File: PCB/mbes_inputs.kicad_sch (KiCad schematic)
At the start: 10 parts

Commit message: PCB-A size reducing
Now PCB-B and PCB-A fits almost perfectly, but not the pin-header connectors. I will use wires instead. But they can be mnounted A on top of B ;-)
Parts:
- Bike_stand1, Decomp_1, LightOnOff_sw1, addLights1, powerOFF1: footprint Connector_Wire:SolderWire-0.5sqmm_1x02_P4.6mm_D0.9mm_OD2.1mm -> Connector_Wire:SolderWire-0.25sqmm_1x02_P4.2mm_D0.65mm_OD1.7mm
- leftCtrls_conn1: footprint Connector_Wire:SolderWire-0.5sqmm_1x06_P4.6mm_D0.9mm_OD2.1mm -> Connector_Wire:SolderWire-0.25sqmm_1x06_P4.5mm_D0.65mm_OD2mm
- rightCtrls_conn1: footprint Connector_Wire:SolderWire-0.5sqmm_1x06_P4.6mm_D0.9mm_OD2.1mm -> Connector_Wire:SolderWire-0.25sqmm_1x06_P4.2mm_D0.65mm_OD1.7mm
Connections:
- net GND: now also powerOFF1.1 (Pin_1)
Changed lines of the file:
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@@
   (junction (at 65.786 67.564) (diameter 0) (color 0 0 0 0)
   )
+  (junction (at 65.7606 148.9456) (diameter 0) (color 0 0 0 0)
+  )
   (junction (at 98.298 135.89) (diameter 0) (color 0 0 0 0)
   )
@@
     (stroke (width 0) (type default))
   )
+  (wire (pts (xy 65.7606 148.9456) (xy 65.786 148.9456))
+    (stroke (width 0) (type default))
+  )
   (wire (pts (xy 93.472 121.793) (xy 95.504 121.793))
     (stroke (width 0) (type default))
@@
     (stroke (width 0) (type default))
   )
-  (wire (pts (xy 65.786 122.428) (xy 65.786 148.9964))
-    (stroke (width 0) (type default))
-  )
-  (wire (pts (xy 61.6712 148.9456) (xy 65.786 148.9456))
+  (wire (pts (xy 65.786 122.428) (xy 65.786 148.9456))
+    (stroke (width 0) (type default))
+  )
+  (wire (pts (xy 61.6712 148.9456) (xy 65.7606 148.9456))
     (stroke (width 0) (type default))
   )
@@
       (effects (font (size 1.27 1.27)) hide)
     )
-    (property "Footprint" "Connector_Wire:SolderWire-0.5sqmm_1x02_P4.6mm_D0.9mm_OD2.1mm" (at 56.642 67.564 0)
+    (property "Footprint" "Connector_Wire:SolderWire-0.25sqmm_1x02_P4.2mm_D0.65mm_OD1.7mm" (at 56.642 67.564 0)
       (effects (font (size 1.27 1.27)) hide)
     )
@@
       (effects (font (size 1.27 1.27)) (justify left) hide)
     )
-    (property "Footprint" "Connector_Wire:SolderWire-0.5sqmm_1x02_P4.6mm_D0.9mm_OD2.1mm" (at 56.896 116.84 0)
+    (property "Footprint" "Connector_Wire:SolderWire-0.25sqmm_1x02_P4.2mm_D0.65mm_OD1.7mm" (at 56.896 116.84 0)
       (effects (font (size 1.27 1.27)) hide)
     )
@@
     )
   )
-  (symbol (lib_id "power:GND") (at 65.786 148.9964 0) (unit 1)
+  (symbol (lib_id "power:GND") (at 65.7606 148.9456 0) (unit 1)
     (in_bom yes) (on_board yes) (dnp no) (fields_autoplaced)
-    (property "Reference" "#PWR0108" (at 65.786 155.3464 0)
-      (effects (font (size 1.27 1.27)) hide)
-    )
-    (property "Value" "GND" (at 65.786 154.0764 0)
-      (effects (font (size 1.27 1.27)))
-    )
-    (property "Footprint" "" (at 65.786 148.9964 0)
-      (effects (font (size 1.27 1.27)) hide)
-    )
-    (property "Datasheet" "" (at 65.786 148.9964 0)
+    (property "Reference" "#PWR0108" (at 65.7606 155.2956 0)
+      (effects (font (size 1.27 1.27)) hide)
+    )
+    (property "Value" "GND" (at 65.7606 154.0256 0)
+      (effects (font (size 1.27 1.27)))
+    )
+    (property "Footprint" "" (at 65.7606 148.9456 0)
+      (effects (font (size 1.27 1.27)) hide)
+    )
+    (property "Datasheet" "" (at 65.7606 148.9456 0)
       (effects (font (size 1.27 1.27)) hide)
     )
@@
       (effects (font (size 1.27 1.27)))
     )
-    (property "Footprint" "Connector_Wire:SolderWire-0.5sqmm_1x06_P4.6mm_D0.9mm_OD2.1mm" (at 56.642 83.312 0)
+    (property "Footprint" "Connector_Wire:SolderWire-0.25sqmm_1x06_P4.5mm_D0.65mm_OD2mm" (at 56.642 83.312 0)
       (effects (font (size 1.27 1.27)) hide)
     )
@@
       (effects (font (size 1.27 1.27)) (justify left) hide)
     )
-    (property "Footprint" "Connector_Wire:SolderWire-0.5sqmm_1x02_P4.6mm_D0.9mm_OD2.1mm" (at 56.642 100.584 0)
+    (property "Footprint" "Connector_Wire:SolderWire-0.25sqmm_1x02_P4.2mm_D0.65mm_OD1.7mm" (at 56.642 100.584 0)
       (effects (font (size 1.27 1.27)) hide)
     )
@@
       (effects (font (size 1.27 1.27)) hide)
     )
-    (property "Footprint" "Connector_Wire:SolderWire-0.5sqmm_1x02_P4.6mm_D0.9mm_OD2.1mm" (at 56.896 122.428 0)
+    (property "Footprint" "Connector_Wire:SolderWire-0.25sqmm_1x02_P4.2mm_D0.65mm_OD1.7mm" (at 56.896 122.428 0)
       (effects (font (size 1.27 1.27)) hide)
     )
@@
       (effects (font (size 1.27 1.27)))
     )
-    (property "Footprint" "Connector_Wire:SolderWire-0.5sqmm_1x06_P4.6mm_D0.9mm_OD2.1mm" (at 56.642 50.292 0)
+    (property "Footprint" "Connector_Wire:SolderWire-0.25sqmm_1x06_P4.2mm_D0.65mm_OD1.7mm" (at 56.642 50.292 0)
       (effects (font (size 1.27 1.27)) hide)
     )
@@
       (effects (font (size 1.27 1.27)) (justify left) hide)
     )
-    (property "Footprint" "Connector_Wire:SolderWire-0.5sqmm_1x02_P4.6mm_D0.9mm_OD2.1mm" (at 56.5912 148.9456 0)
-      (effects (font (size 1.27 1.27)) hide)
-    )
+    (property "Footprint" "Connector_Wire:SolderWire-0.25sqmm_1x02_P4.2mm_D0.65mm_OD1.7mm" (at 56.5912 148.9456 0)
+      (effects (font (size 1.27 1.27)) hide)
+    )

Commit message: Size reducing and component rationalization
- RS232(TTL) lines on PCB-B have been removed (MAX232 is already mounted in PCB-A)
- The two PCB can no more be connected using pin-header connectors. You have to use welded wires, now.
  (this solution is not beautiful as the original, but it is a more flexible one and it also allowd me
  to reduce the PCB size)

The PCBs size is approximately 109.7mm x 43.5mm.
For this dual-face sigle-layer (THT) version this is the minimum size I can achieve.
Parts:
- Bike_stand1, Decomp_1, LightOnOff_sw1, addLights1, powerOFF1: footprint Connector_Wire:SolderWire-0.25sqmm_1x02_P4.2mm_D0.65mm_OD1.7mm -> Connector_Wire:SolderWire-0.15sqmm_1x02_P4mm_D0.5mm_OD1.5mm
- leftCtrls_conn1: footprint Connector_Wire:SolderWire-0.25sqmm_1x06_P4.5mm_D0.65mm_OD2mm -> Connector_Wire:SolderWire-0.25sqmm_1x06_P4.2mm_D0.65mm_OD1.7mm
- rightCtrls_conn1: footprint Connector_Wire:SolderWire-0.25sqmm_1x06_P4.2mm_D0.65mm_OD1.7mm -> Connector_Wire:SolderWire-0.15sqmm_1x06_P4mm_D0.5mm_OD1.5mm

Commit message: Tuning and fixes
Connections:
- net i_Vx1: now also Key-locker-1.3 (Pin_3); no longer Key-locker-1.2 (Pin_2)
- net i_Vx2: now also Key-locker-1.1 (Pin_1); no longer Key-locker-1.4 (Pin_4)
- new net: Key-locker-1.2 (Pin_2), Key-locker-1.4 (Pin_4), R1.2
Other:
- moved on the sheet: Key-locker-1
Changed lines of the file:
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@@
 	(symbol
 		(lib_id "Connector_Generic:Conn_01x04")
-		(at 56.896 133.35 0)
-		(mirror y)
+		(at 56.896 135.89 180)
 		(unit 1)
 		(exclude_from_sim no)
@@
 		(dnp no)
 		(property "Reference" "Key-locker-1"
-			(at 57.3532 128.1176 0)
+			(at 56.642 128.016 0)
 			(effects
 				(font
@@
 		)
 		(property "Value" "Conn_01x04"
-			(at 56.896 142.5956 0)
+			(at 56.896 126.6444 0)
 			(effects
 				(font
@@
 		)
 		(property "Footprint" "Connector_PinHeader_2.54mm:PinHeader_1x04_P2.54mm_Vertical"
-			(at 56.896 133.35 0)
+			(at 56.896 135.89 0)
 			(effects
 				(font
@@
 		)
 		(property "Datasheet" "~"
-			(at 56.896 133.35 0)
+			(at 56.896 135.89 0)
 			(effects
 				(font
@@
 		)
 		(property "Description" ""
-			(at 56.896 133.35 0)
+			(at 56.896 135.89 0)
 			(effects
 				(font

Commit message: Important fixes and adjustments
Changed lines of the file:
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@@
-	)
-	(junction
-		(at 98.298 135.89)
-		(diameter 0)
-		(color 0 0 0 0)
 	)
 	(junction
@@
 	(wire
 		(pts
-			(xy 75.946 135.89) (xy 98.298 135.89)
-		)
-		(stroke
-			(width 0)
-			(type default)
-		)
-	)
-	(wire
-		(pts
 			(xy 91.44 133.35) (xy 91.44 118.491)
 		)
@@
 	(wire
 		(pts
-			(xy 98.298 135.89) (xy 101.727 135.89)
+			(xy 75.946 135.89) (xy 101.727 135.89)
 		)
 		(stroke
@@
 					(unit 1)
 				)
-			)
-		)
-	)
-	(symbol
-		(lib_id "power:PWR_FLAG")
-		(at 98.298 135.89 0)
-		(unit 1)
-		(exclude_from_sim no)
-		(in_bom yes)
-		(on_board yes)
-		(dnp no)
-		(fields_autoplaced yes)
-		(property "Reference" "#FLG0103"
-			(at 98.298 133.985 0)
-			(effects
-				(font
-					(size 1.27 1.27)
-				)
-				(hide yes)
-			)
-		)
-		(property "Value" "PWR_FLAG"
-			(at 98.298 131.318 0)
-			(effects
-				(font
-					(size 1.27 1.27)
-				)
-			)
-		)
-		(property "Footprint" ""
-			(at 98.298 135.89 0)
-			(effects
-				(font
-					(size 1.27 1.27)
-				)
-				(hide yes)
-			)
-		)
-		(property "Datasheet" "~"
-			(at 98.298 135.89 0)
-			(effects
-				(font
-					(size 1.27 1.27)
-				)
-				(hide yes)
-			)
-		)
-		(property "Description" ""
-			(at 98.298 135.89 0)
-			(effects
-				(font
-					(size 1.27 1.27)
-				)
-				(hide yes)
-			)
-		)
-		(pin "1"
-		)
-		(instances
-			(project "pcb-a"
-				(path "/709d0967-afe5-49d3-92a5-d2bb94550bdb/0b22d592-b723-42a2-89dd-bec665c2bd26"
-					(reference "#FLG0103")
-					(unit 1)
-				)

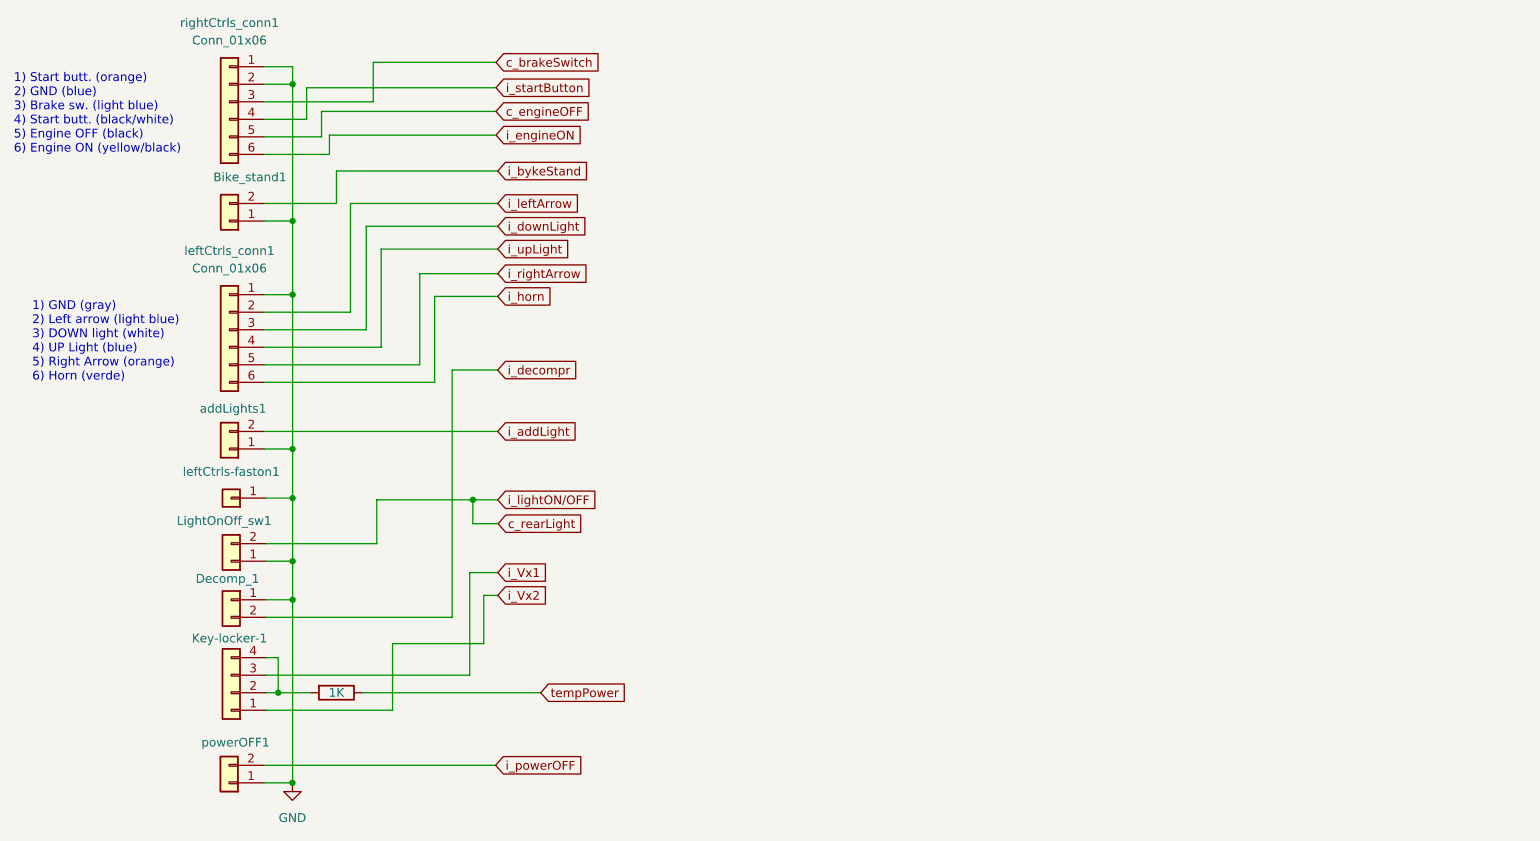
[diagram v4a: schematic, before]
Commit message: Bike-stand switch moved in the rear-connector
All connectors have been placed in one single sheet
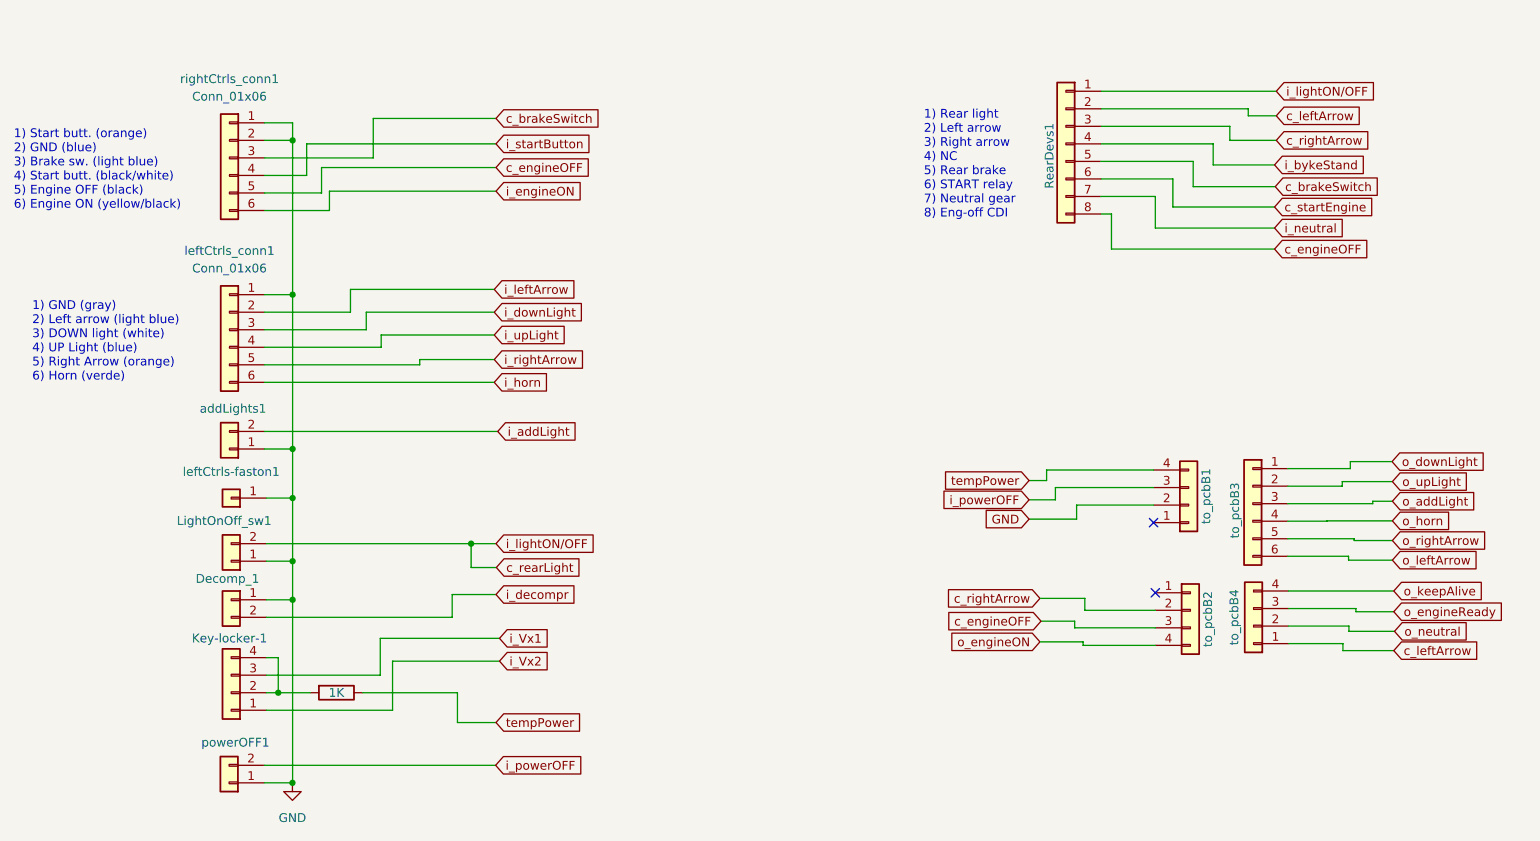
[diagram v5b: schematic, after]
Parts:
- removed Bike_stand1: Conn_01x02, Connector_Wire:SolderWire-0.15sqmm_1x02_P4mm_D0.5mm_OD1.5mm, symbol Connector_Generic:Conn_01x02
- added RearDevs1: Conn_01x08, Connector_PinHeader_2.54mm:PinHeader_1x08_P2.54mm_Vertical, symbol Connector_Generic:Conn_01x08
- added to_pcbB1, to_pcbB2, to_pcbB4: Conn_01x04, Connector_PinHeader_2.54mm:PinHeader_1x04_P2.54mm_Vertical, symbol Connector_Generic:Conn_01x04
- added to_pcbB3: Conn_01x06, Connector_PinHeader_2.54mm:PinHeader_1x06_P2.54mm_Vertical, symbol Connector_Generic:Conn_01x06
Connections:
- net GND: now also to_pcbB1.2 (Pin_2)
- net c_brakeSwitch: now also RearDevs1.5 (Pin_5)
- net c_engineOFF: now also RearDevs1.8 (Pin_8), to_pcbB2.3 (Pin_3)
- net c_rearLight: now also RearDevs1.1 (Pin_1)
- net i_bykeStand: now also RearDevs1.4 (Pin_4)
- net i_powerOFF: now also to_pcbB1.3 (Pin_3)
- net tempPower: now also to_pcbB1.4 (Pin_4)
- new net c_leftArrow: RearDevs1.2 (Pin_2), to_pcbB4.1 (Pin_1)
- new net c_rightArrow: RearDevs1.3 (Pin_3), to_pcbB2.2 (Pin_2)
- new net c_startEngine: RearDevs1.6 (Pin_6)
- new net i_neutral: RearDevs1.7 (Pin_7)
- new net o_addLight: to_pcbB3.3 (Pin_3)
- new net o_downLight: to_pcbB3.1 (Pin_1)
- new net o_engineON: to_pcbB2.4 (Pin_4)
- new net o_engineReady: to_pcbB4.3 (Pin_3)
- new net o_horn: to_pcbB3.4 (Pin_4)
- new net o_keepAlive: to_pcbB4.4 (Pin_4)
- new net o_leftArrow: to_pcbB3.6 (Pin_6)
- new net o_neutral: to_pcbB4.2 (Pin_2)
- new net o_rightArrow: to_pcbB3.5 (Pin_5)
- new net o_upLight: to_pcbB3.2 (Pin_2)
- no-connect marks 0 -> 2
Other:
- note added: "1) Rear light 2) Left arrow 3) Right arrow 4) NC 5) Rear brake 6) START relay 7) Neutral gear 8) Eng-off CDI"
- title: Motorbike lights and services controller -> All the pcb's connectors
- moved on the sheet: rightCtrls_conn1
